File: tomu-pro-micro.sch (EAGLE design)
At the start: 18 parts, among them U1 EFM32HG309F64G

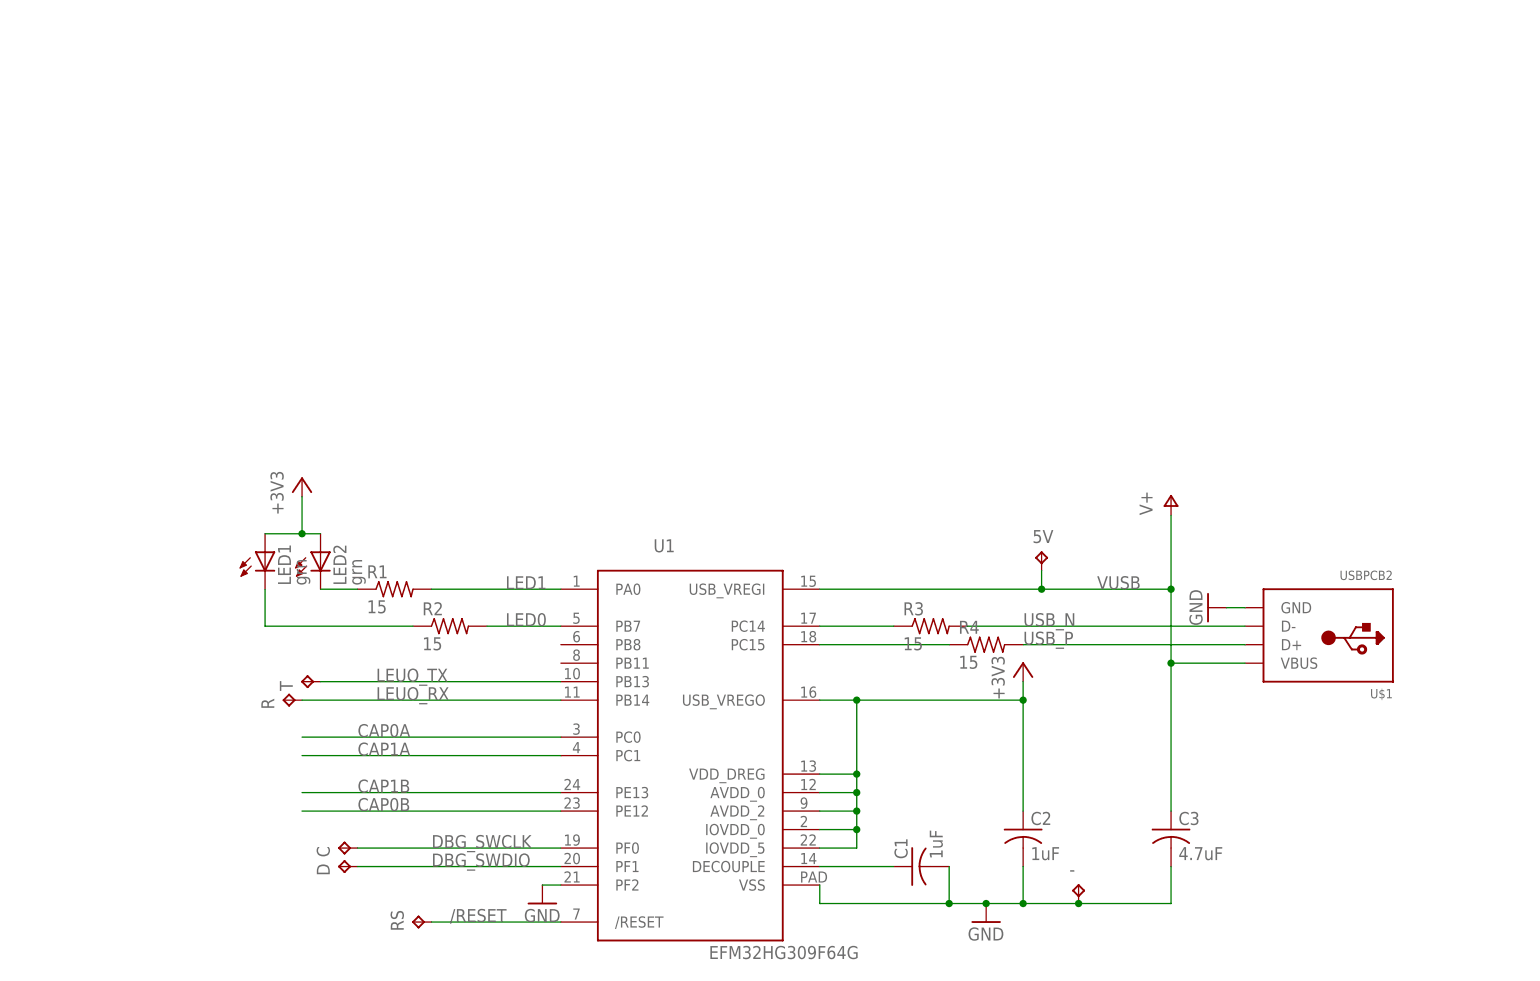
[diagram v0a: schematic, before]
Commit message: added tomo-pro-micro breakout board
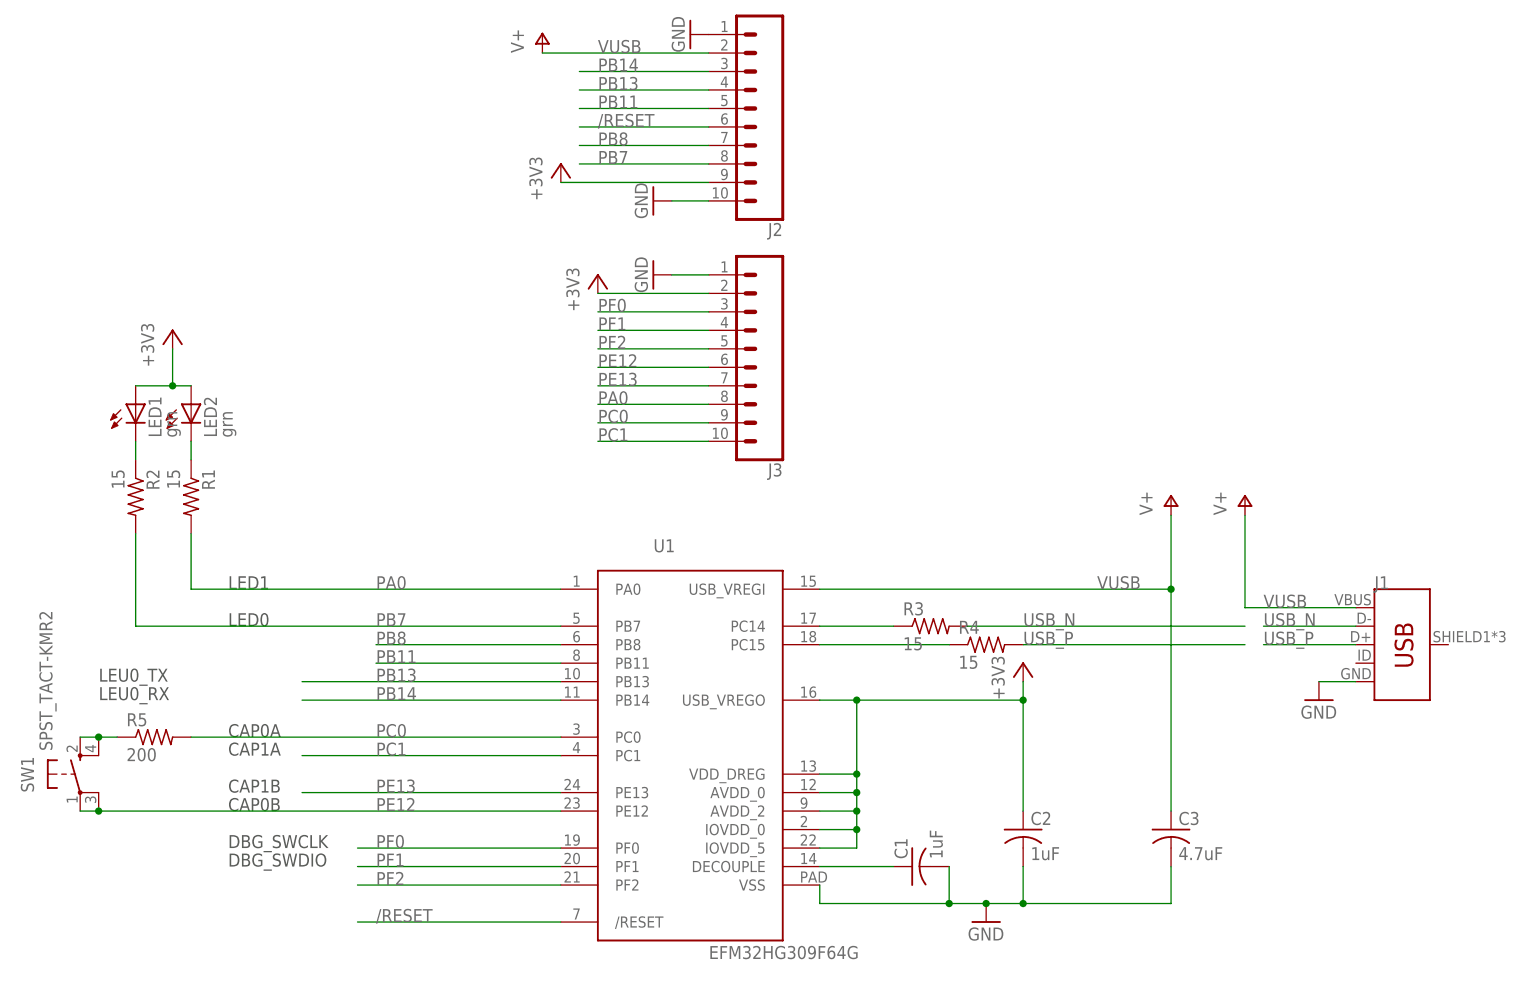
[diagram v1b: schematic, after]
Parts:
- removed -: TPTP10SQ, testpad:TPTP10SQ
- removed 5V, C, D, R, RS, T: TPTP10R, testpad:TPTP10R
- removed U$1: USBPCB2, todstuff:USBPCB2
- added J1: (no value), SparkFun-Connectors:USB_MICRO-B_FEMALE-SMT
- added J2, J3: (no value), SparkFun-Connectors:CONN_10"
- added R5: 200, adafruit:R-US_R0603
- added SW1: SPST_TACT-KMR2, adafruit:SPST_TACT-KMR2
- C1: device adafruit:C-USC0402K -> adafruit:C-USC0603
- C2, C3: device adafruit:C-USC0402 -> adafruit:C-USC0603
- R1, R2, R3, R4: device adafruit:R-US_R0402 -> adafruit:R-US_R0603
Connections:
- removed net CAP0A: U1.PC0
- removed net CAP0B: U1.PE12
- removed net CAP1A: U1.PC1
- removed net CAP1B: U1.PE13
- removed net DBG_SWCLK: C.TP, U1.PF0
- removed net DBG_SWDIO: D.TP, U1.PF1
- removed net LED0: R2.2, U1.PB7
- removed net LED1: R1.2, U1.PA0
- removed net LEUO_RX: R.TP, U1.PB14
- removed net LEUO_TX: T.TP, U1.PB13
- new net N$20: R5.1, SW1.S, SW1.S1
- new net PA0: J3.8, R1.2, U1.PA0
- new net PB11: J2.5, U1.PB11
- new net PB13: J2.4, U1.PB13
- new net PB14: J2.3, U1.PB14
- new net PB7: J2.8, R2.2, U1.PB7
- new net PB8: J2.7, U1.PB8
- new net PC0: J3.9, R5.2, U1.PC0
- new net PC1: J3.10, U1.PC1
- new net PE12: J3.6, SW1.P, SW1.P1, U1.PE12
- new net PE13: J3.7, U1.PE13
- new net PF0: J3.3, U1.PF0
- new net PF1: J3.4, U1.PF1
- new net PF2: J3.5, U1.PF2
- net +3V3: now also J2.9, J3.2
- net /RESET: now also J2.6; no longer RS.TP
- net GND: now also J1.GND, J2.1, J2.10, J3.1; no longer -.TP, U$1.GND, U1.PF2
- net USB_N: now also J1.D-; no longer U$1.D-
- net USB_P: now also J1.D+; no longer U$1.D+
- net VUSB: now also J1.VBUS, J2.2; no longer 5V.TP, U$1.VBUS
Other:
- note added: "CAP0A"
- note added: "CAP0B"
- note added: "CAP1A"
- note added: "CAP1B"
- note added: "DBG_SWCLK"
- note added: "DBG_SWDIO"
- note added: "LED0"
- note added: "LED1"
- note added: "LEU0_RX"
- note added: "LEU0_TX"
- moved on the sheet: LED1, LED2, R1, R2

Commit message: LED resistors should be 75 not 15 (or maybe 52 as in the tomu bom)
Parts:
- R1, R2: value 15 -> 75
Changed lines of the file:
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@@
 <part name="GND3" library="supply1" library_urn="urn:adsk.eagle:library:371" deviceset="GND" device=""/>
 <part name="+3V2" library="supply1" library_urn="urn:adsk.eagle:library:371" deviceset="+3V3" device=""/>
-<part name="R1" library="adafruit" library_urn="urn:adsk.eagle:library:420" deviceset="R-US_" device="R0603" value="15"/>
-<part name="R2" library="adafruit" library_urn="urn:adsk.eagle:library:420" deviceset="R-US_" device="R0603" value="15"/>
+<part name="R1" library="adafruit" library_urn="urn:adsk.eagle:library:420" deviceset="R-US_" device="R0603" value="75"/>
+<part name="R2" library="adafruit" library_urn="urn:adsk.eagle:library:420" deviceset="R-US_" device="R0603" value="75"/>
 <part name="LED1" library="adafruit" library_urn="urn:adsk.eagle:library:420" deviceset="LED" device="CHIP-LED0603" value="grn"/>
 <part name="LED2" library="adafruit" library_urn="urn:adsk.eagle:library:420" deviceset="LED" device="CHIP-LED0603" value="grn"/>
